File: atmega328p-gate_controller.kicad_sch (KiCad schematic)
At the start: 23 parts, among them J1 CONN, J10 PWR, J11 Conn_02x04_Counter_Clockwise, J12 UART, J17 JMP, J18 ISP/SPI, J2 JMP, J4 Conn_02x04_Counter_Clockwise, J5 5V, J6 3V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

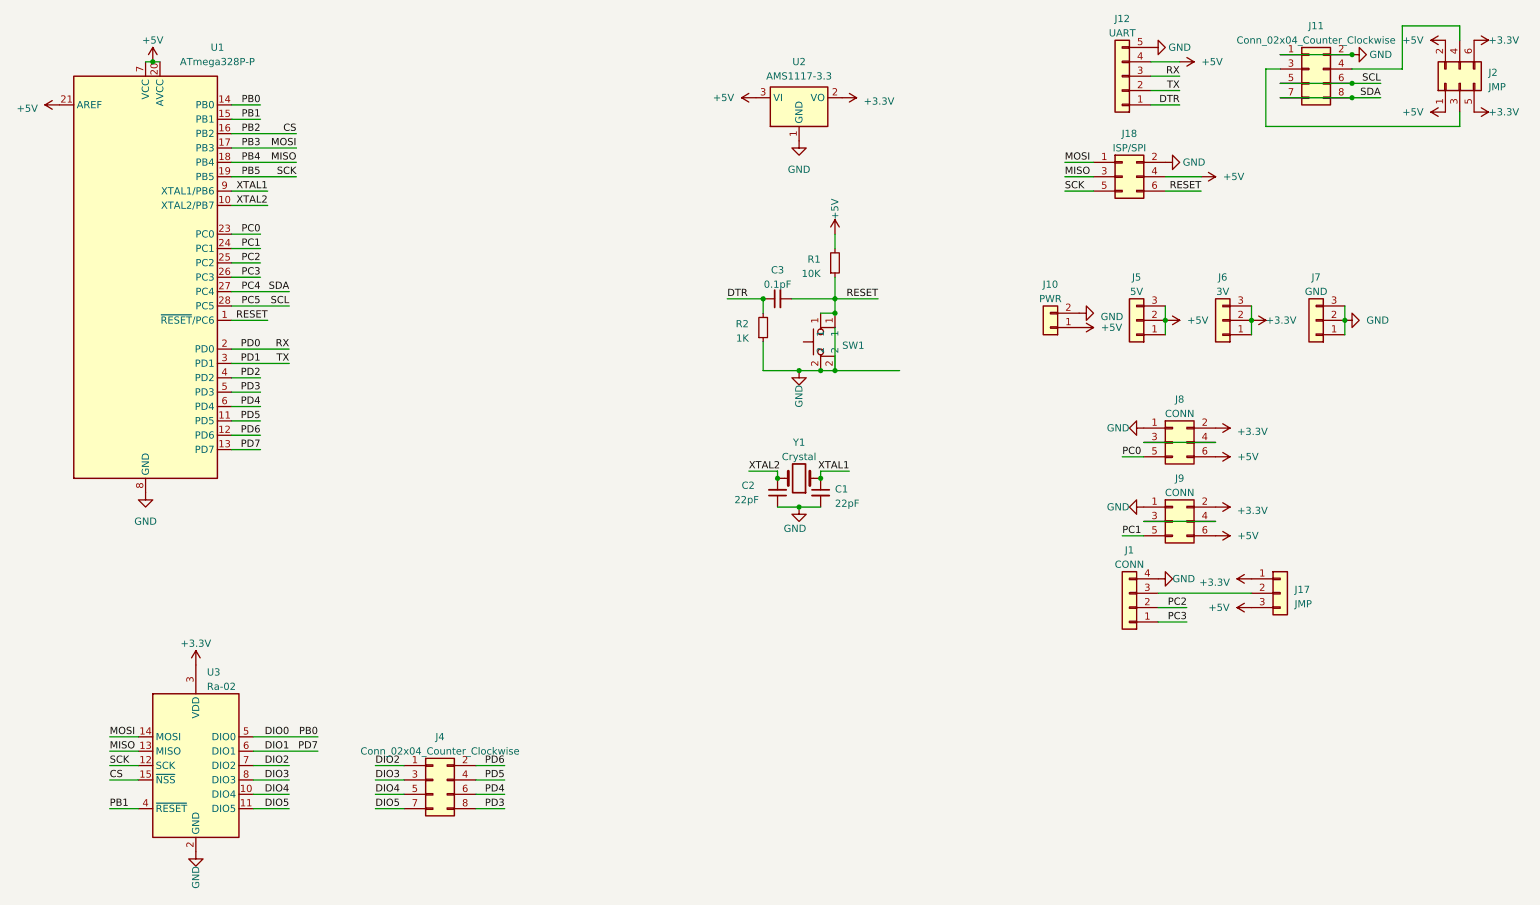
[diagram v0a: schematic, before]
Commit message: silkscreen done
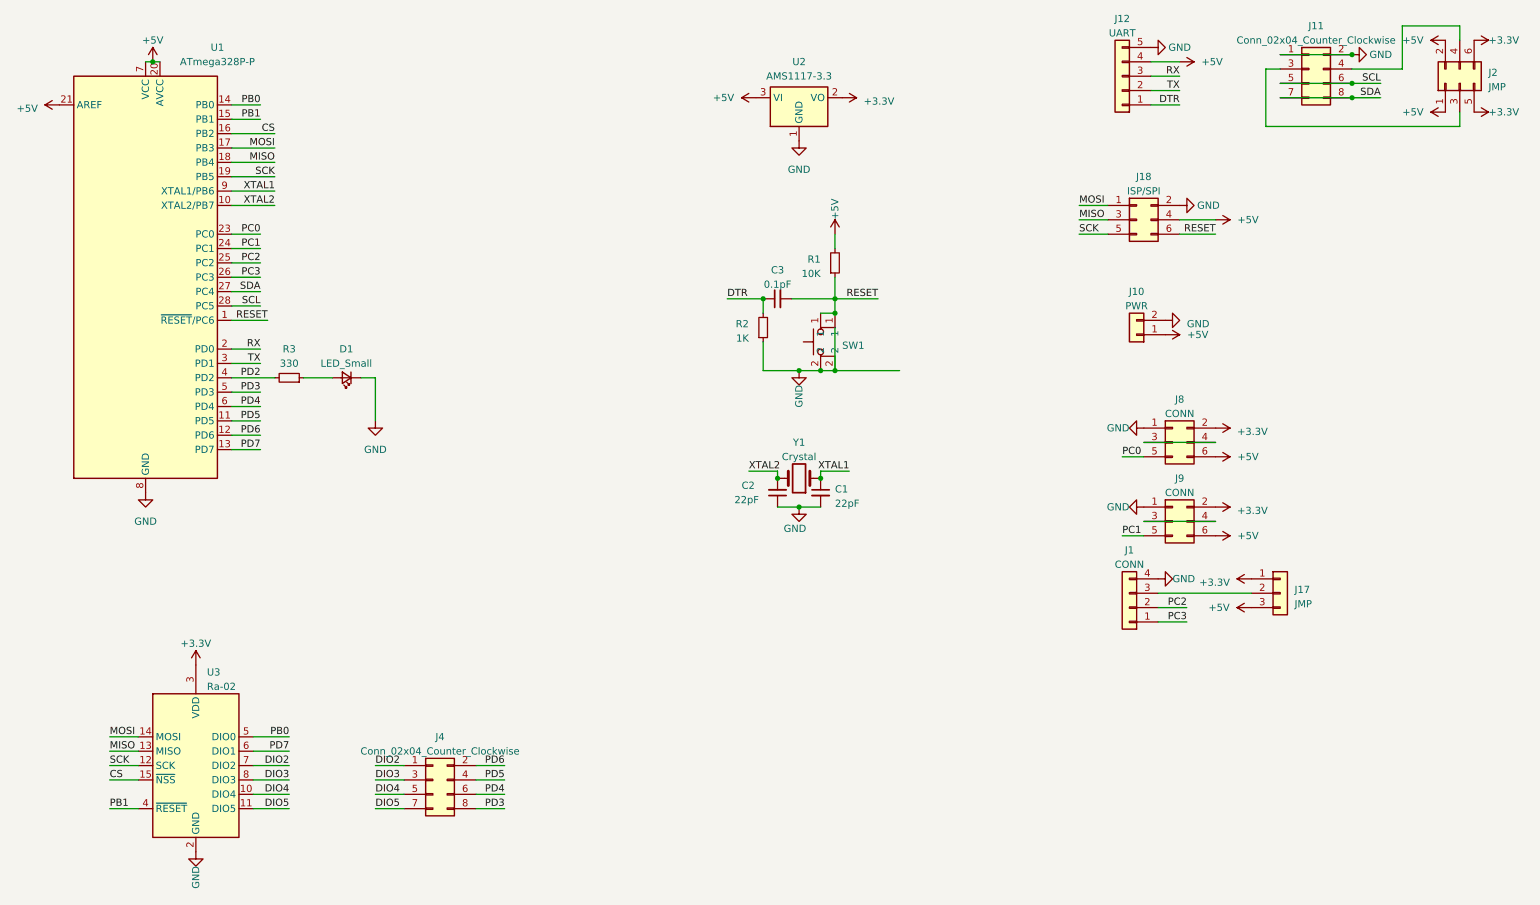
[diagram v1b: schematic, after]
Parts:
- removed J5: 5V, Connector_PinHeader_2.54mm:PinHeader_1x03_P2.54mm_Vertical, symbol Connector_Generic:Conn_01x03
- removed J6: 3V, Connector_PinHeader_2.54mm:PinHeader_1x03_P2.54mm_Vertical, symbol Connector_Generic:Conn_01x03
- removed J7: GND, Connector_PinHeader_2.54mm:PinHeader_1x03_P2.54mm_Vertical, symbol Connector_Generic:Conn_01x03
- added D1: LED_Small, LED_SMD:LED_0603_1608Metric_Pad1.05x0.95mm_HandSolder, symbol Device:LED_Small
- added R3: 330, Resistor_SMD:R_0603_1608Metric_Pad0.98x0.95mm_HandSolder, symbol Device:R_Small
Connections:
- net GND: now also D1.1 (K)
- net PD2: now also R3.2
- net DIO0 renamed PB0
- net DIO1 renamed PD7
- net PB5 renamed SCK
- net PC4 renamed SDA
- net PC5 renamed SCL
- net PD0 renamed RX
- net PD1 renamed TX
- new net: D1.2 (A), R3.1
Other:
- moved on the sheet: J10, J18
